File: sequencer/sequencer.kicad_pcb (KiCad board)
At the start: 2 copper layers, 53.3 x 86.5 mm, 44 parts, among them J1 Conn_01x05_Male, J2 AudioJack3_Ground, J4 Conn_02x05_Odd_Even, SW1 Rotary_Encoder, U1 PIC16F690-IP, U2 4051, U3 TL072, U4 L7805

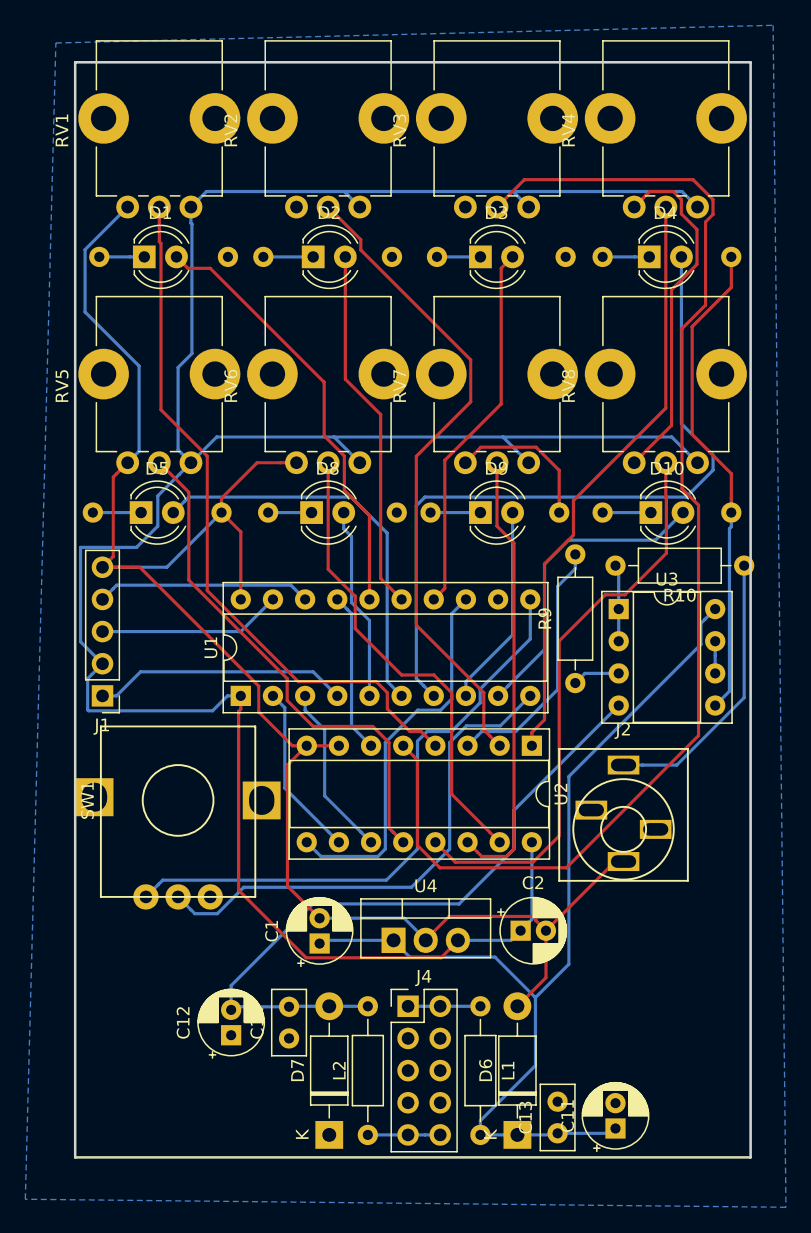
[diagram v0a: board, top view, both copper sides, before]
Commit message: Added gate to sequencer
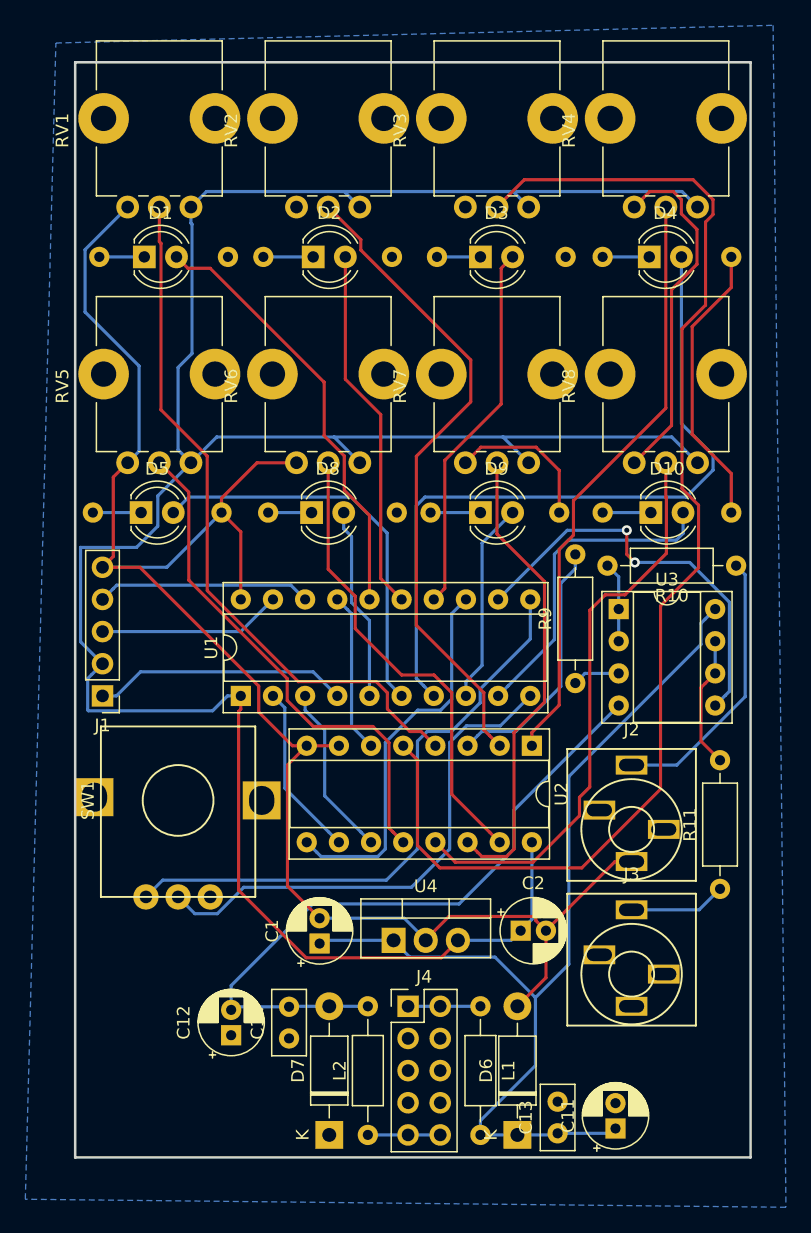
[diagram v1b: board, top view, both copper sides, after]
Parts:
- added J3: Gate, synth:jack_audio, F.Cu at (87.8, 104.6)
- added R11: 100, Resistor_THT:R_Axial_DIN0207_L6.3mm_D2.5mm_P10.16mm_Horizontal, F.Cu at (94.7, 97.9)
- J2: value AudioJack3_Ground -> CV_OUT
- moved J2 0.64 mm to (87.8, 93.2)
- moved R10 0.64 mm to (96.0, 72.4)
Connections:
- U3 pad 5: GND -> Net-(U1-Pad12)
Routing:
- net Net-(U1-Pad12): track 0.00 -> 32.6 mm, vias 0 -> 2
- net GND: track 214.4 -> 199.9 mm
- net Net-(R11-Pad2): track 2.54 -> 10.5 mm
- net Net-(J3-PadT): track 0.00 -> 7.67 mm
- net Net-(RV7-Pad2): track 35.4 -> 37.4 mm
- net Net-(D10-Pad2): track 24.6 -> 25.5 mm
- net Net-(RV3-Pad2): track 98.1 -> 98.8 mm

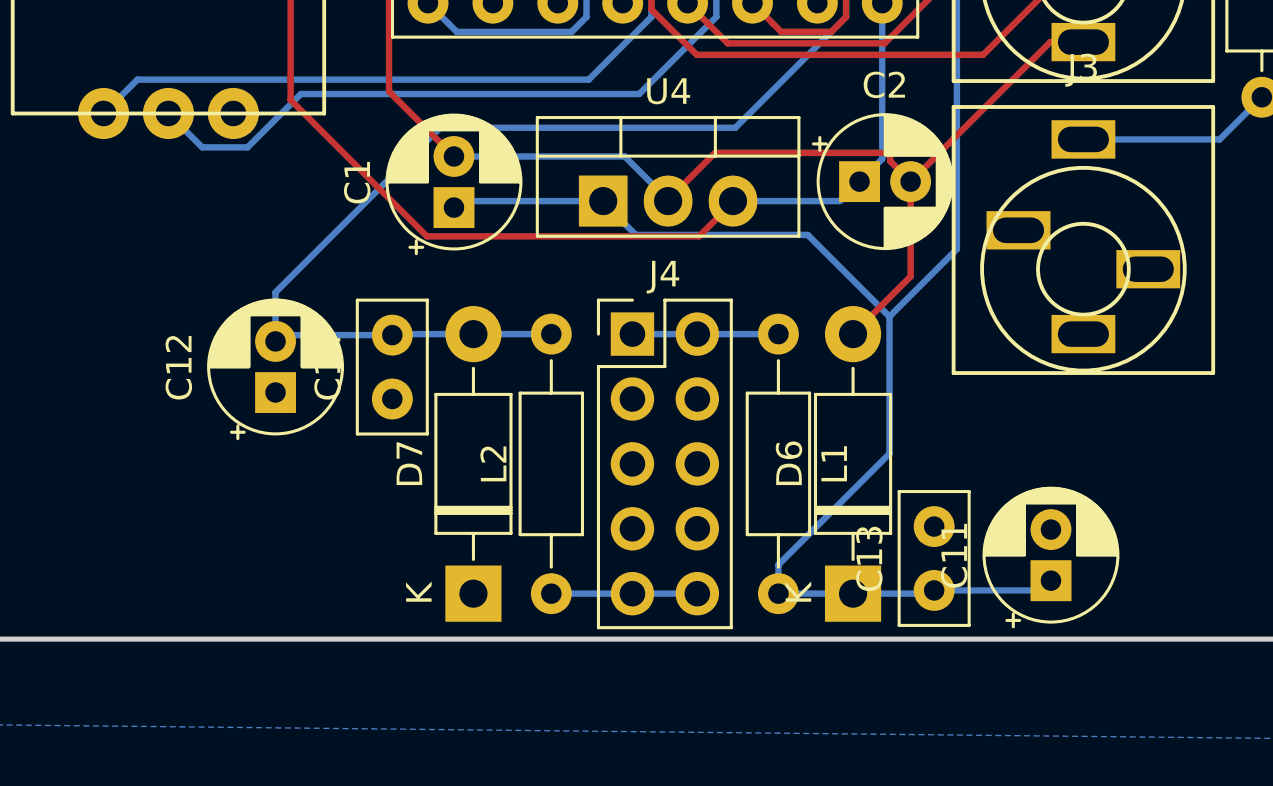
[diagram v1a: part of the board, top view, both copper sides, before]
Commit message: Modified the eurorackpin schematic and cleaned up
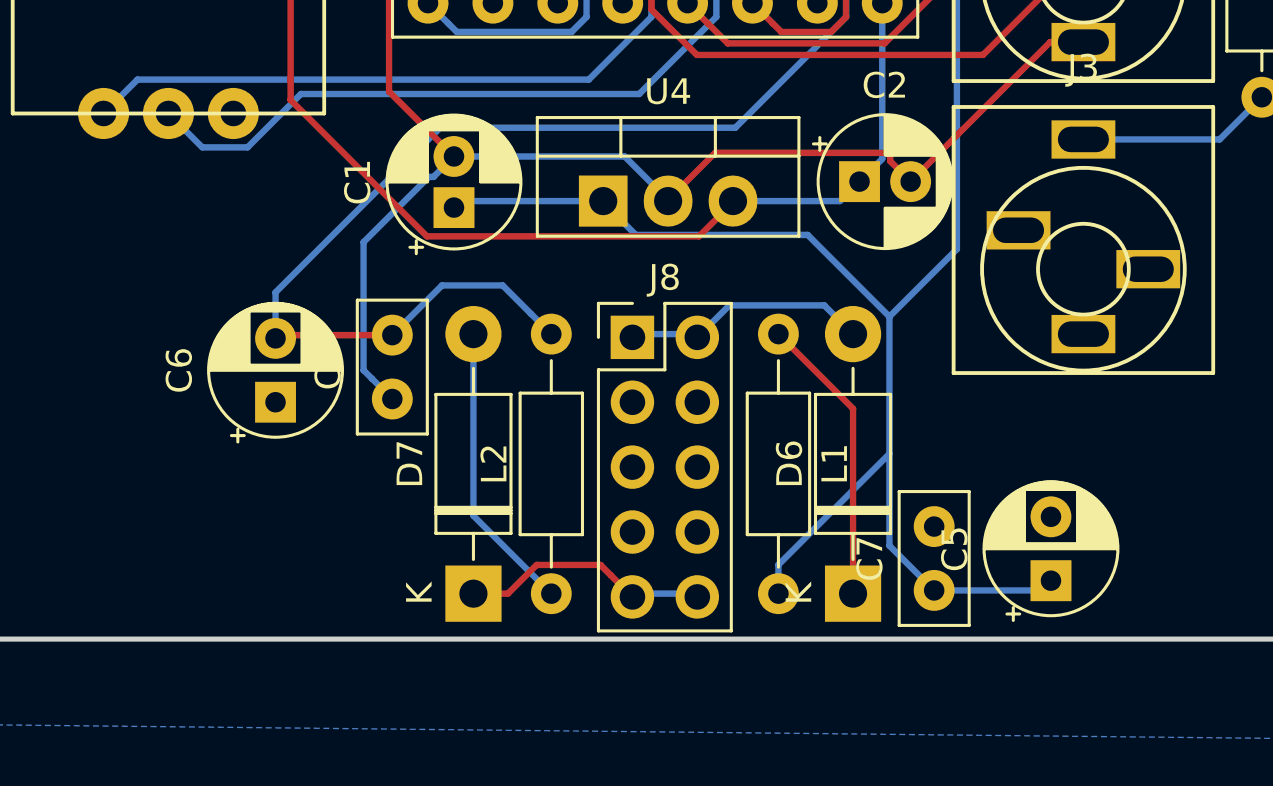
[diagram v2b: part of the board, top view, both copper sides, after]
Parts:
- removed C11, C12: 10uF, Capacitor_THT:CP_Radial_D5.0mm_P2.00mm
- removed C13, C14: 100nF, Capacitor_THT:C_Disc_D5.0mm_W2.5mm_P2.50mm
- removed J4: Conn_02x05_Odd_Even, Connector_PinHeader_2.54mm:PinHeader_2x05_P2.54mm_Vertical
- added C5: 10uF, Capacitor_THT:CP_Radial_D5.0mm_P2.50mm, F.Cu at (86.5, 116.8)
- added C6: 10uF, Capacitor_THT:CP_Radial_D5.0mm_P2.50mm, F.Cu at (56.1, 109.9)
- added C7: 100nF, Capacitor_THT:C_Disc_D5.0mm_W2.5mm_P2.50mm, F.Cu at (81.9, 117.2)
- added C8: 100nF, Capacitor_THT:C_Disc_D5.0mm_W2.5mm_P2.50mm, F.Cu at (60.7, 109.7)
- added J8: Conn_02x05_Odd_Even, Connector_PinHeader_2.54mm:PinHeader_2x05_P2.54mm_Vertical, F.Cu at (70.1, 107.3)
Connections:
- D6 pad 1: 12V -> /EURORACKPIN/12Vto5V
- D6 pad 2: GND -> 12VC
- D7 pad 1: GND -> -12VC
- D7 pad 2: /EURORACKPIN/-12V -> Net-(D7-Pad2)
- L1 pad 1: 12VC -> /EURORACKPIN/12Vto5V
- L2 pad 1: -12VC -> Net-(D7-Pad2)
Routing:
- net Net-(D7-Pad2): track 0.00 -> 11.4 mm
- net /EURORACKPIN/12Vto5V: track 0.00 -> 11.4 mm
- net GND: track 199.9 -> 204.5 mm
- net -12VC: track 5.72 -> 9.75 mm
- net 12VC: track 5.72 -> 9.62 mm
- net /EURORACKPIN/-12V: track 54.4 -> 56.0 mm
